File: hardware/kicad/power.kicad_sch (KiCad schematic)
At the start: 26 parts, among them J1 Phoenix_MSTBA_2,5/3-G-5,08, Q1 PMV65XP, U1 LM2596S-5.0, U2 TPS62933

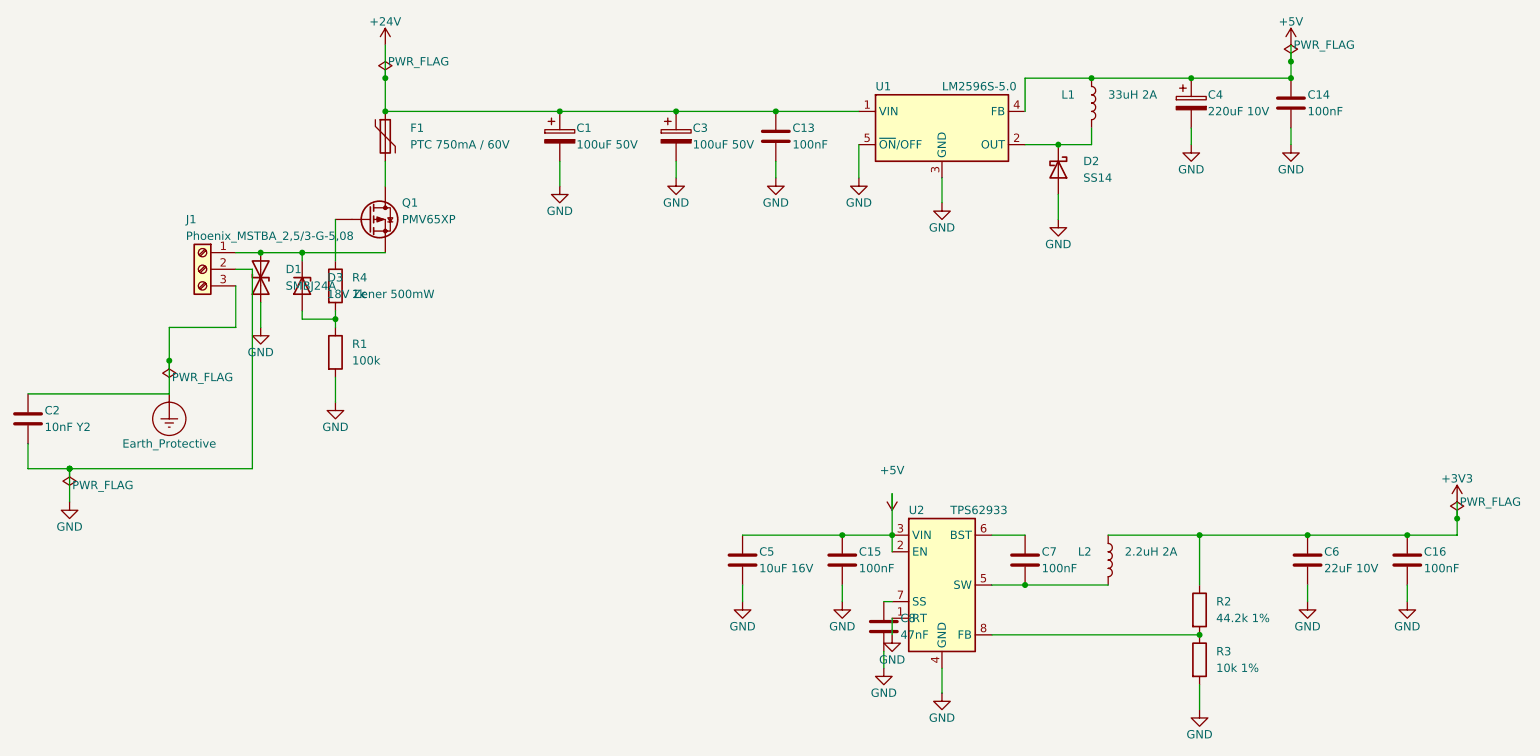
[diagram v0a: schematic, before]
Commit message: kicad+bom: v0.36 - swarm-audit fixes (4 CRITICAL + 3 IMPORTANT)
All 30-agent swarm audit findings from _swarm-audit-v0.35.md addressed.

CRITICAL fixes (would have caused board failure):
- C1 D1 TVS polarity: schematic angle 90→270 AND PCB rotation 0→180
  jointly land KiCad D_SMB pad 1 (cathode) on +24V VIN (was on GND).
  Net renamed Net-(D1-A2) → Net-(D1-A1) in oas_routes.py.
- C2 TPS62933 FB divider: schematic R2 44.2k→100k, R3 10k→30.9k for
  correct Vref=0.8V (was designed against wrong Vref=0.6V assumption).
  Vout = 0.8 × (1 + 100/30.9) = 3.39V (within ±3% of 3.3V target).
- C3 C7/C8 align: PCB-generator C7=22pF/C8=100nF (with swapped BST/SS
  roles) was contradicting the schematic C7=100nF BST + C8=47nF SS.
  Aligned PCB-generator to schematic (correct TPS62933 config).
- C4 Q1 substitution: PMV65XP (Vds=-20V) → AO3401A (LCSC C15127,
  Vds=-30V, same SOT-23 footprint). 8.9V margin over SMBJ24A 38.9V
  clamp. AO3401A drop-in: 1=G, 2=S, 3=D — no PCB layout change.

IMPORTANT fixes:
- I1 silk polarity markers: cathode bar on F.SilkS for D_SMA/D_SMB/
  D_SOD-323 (D1/D2/D3); "+" mark for CP_Radial (C1/C3/C4). Bar X
  computed from pad inner edge so silk clears mask opening by 0.25mm.
- I2 J10 cutout C3 north wall: +28.998 → +27.498 so pad 6 (BOOT)
  fully inside keepout (was 0.7mm outside).
- I3 J2/J10 DNP: (in_bom yes)→(in_bom no) when dnp flag is set.
- I7 D3 value text "500mW" → "200mW" matching BZT52C18S datasheet.

R1 value text aligned "100k" → "100k 1%" for consistent BOM grouping.

Verification: DRC=0, ERC=0, determinism PASS (17 files bit-identical),
Z-clearance PASS (76 footprints), preflight PASS, BOM=12 Basic + 11
Extended SMD + 8 THT (zero unmapped rows).

Co-Authored-By: Claude Opus 4.7 (1M context) <noreply@anthropic.com>
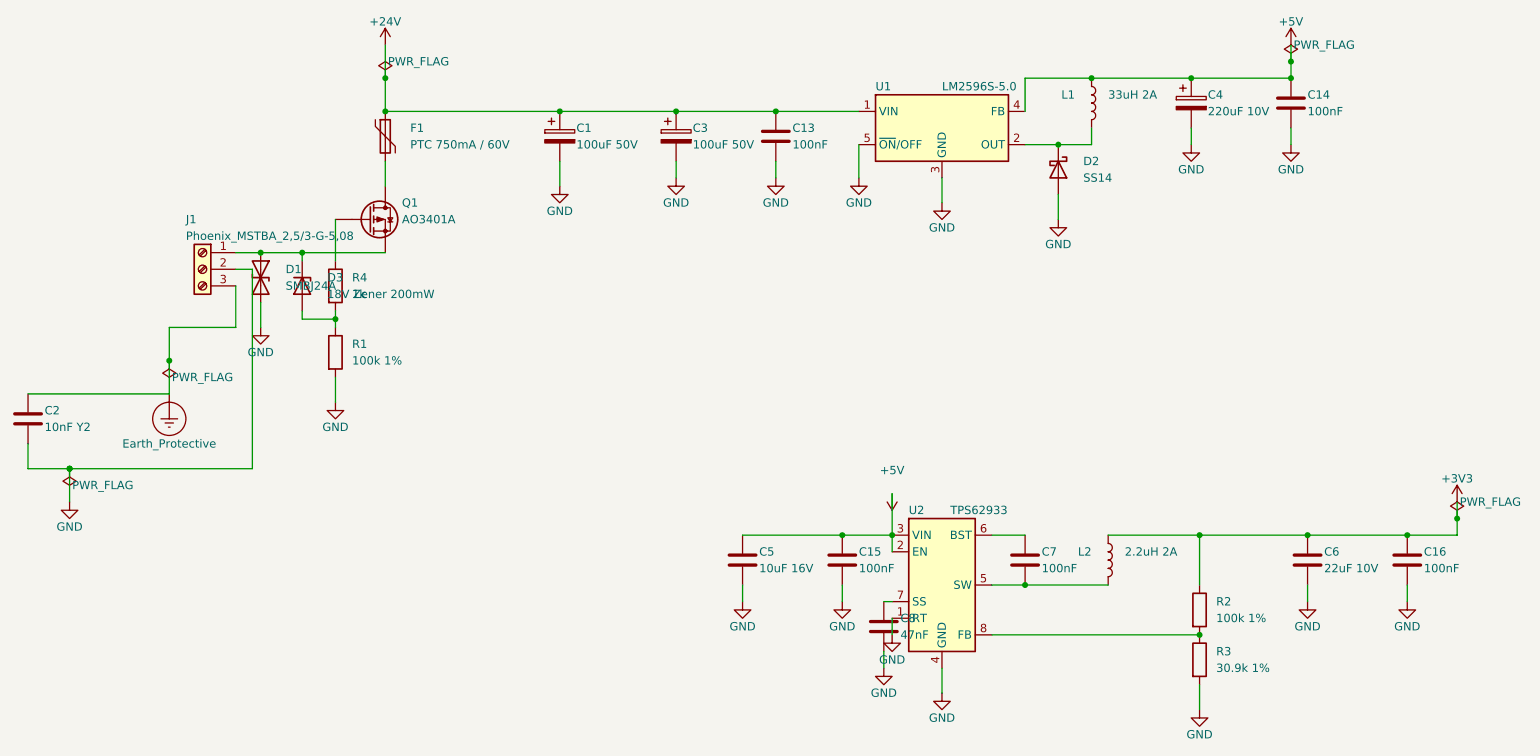
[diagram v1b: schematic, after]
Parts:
- D3: value 18V Zener 500mW -> 18V Zener 200mW
- Q1: value PMV65XP -> AO3401A
- R1: value 100k -> 100k 1%
- R2: value 44.2k 1% -> 100k 1%
- R3: value 10k 1% -> 30.9k 1%
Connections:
- net GND: now also D1.2 (A2); no longer D1.1 (A1)
- net at D3.1 (K), J1.1 (Pin_1), Q1.S: now also D1.1 (A1); no longer D1.2 (A2)
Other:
- moved on the sheet: D1
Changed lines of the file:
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@@
 (symbol
 	(lib_id "Device:D_TVS")
-	(at 66.04 87.63 90)
+	(at 66.04 87.63 270)
 	(unit 1)
 	(exclude_from_sim no)
@@
 	(fields_autoplaced no)
 	(property "Reference" "D1"
-		(at 69.85 86.36 270)
+		(at 69.85 86.36 90)
 		(effects
 			(font
@@
 	)
 	(property "Value" "SMBJ24A"
-		(at 69.85 88.9 270)
+		(at 69.85 88.9 90)
 		(effects
 			(font
@@
 		)
 	)
-	(property "Value" "18V Zener 500mW"
+	(property "Value" "18V Zener 200mW"
 		(at 76.2 90.17 90)
 		(effects
@@
 		)
 	)
-	(property "Value" "PMV65XP"
+	(property "Value" "AO3401A"
 		(at 87.63 78.74 0)
 		(effects
@@
 		)
 	)
-	(property "Value" "100k"
+	(property "Value" "100k 1%"
 		(at 80.01 100.33 0)
 		(effects
@@
 		)
 	)
-	(property "Value" "44.2k 1%"
+	(property "Value" "100k 1%"
 		(at 212.09 139.7 0)
 		(effects
@@
 		)
 	)
-	(property "Value" "10k 1%"
+	(property "Value" "30.9k 1%"
 		(at 212.09 147.32 0)
 		(effects

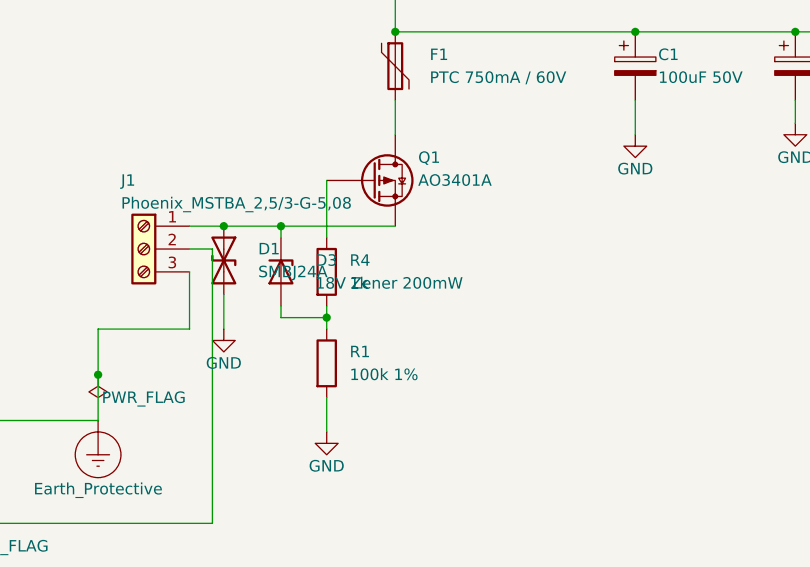
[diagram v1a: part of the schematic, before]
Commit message: kicad+bom: v0.37 - D3 Zener 18V→10V (AO3401A Vgs protection)
Re-audit found AO3401A Vgs_max=±12V (verified aosmd.com), NOT ±20V as
the v0.36 fix description assumed (which carried over the wrong value
from the original PMV65XP comments). The 18V Zener D3 would have clamped
Vgs at -18V, exceeding AO3401A's ±12V rating by 6V — same Vgs overstress
problem the original audit #13 flagged for PMV65XP, not actually solved
by the substitution.

Fix: D3 18V → 10V Zener (BZT52C10S, LCSC C8492). Now Vgs = -10V:
  - 2V margin under AO3401A's ±12V Vgs_max
  - Optimal Rds_on operating point: 45 mΩ at Vgs=-10V per AO3401A datasheet

Steady-state Pz = (24-10)/1k × 10V = 140 mW within SOD-323 200 mW rating
(1.43× margin).

DRC=0, ERC=0, determinism PASS, Z-clearance PASS (76 footprints),
preflight PASS, BOM 12 Basic + 11 Extended + 8 THT unchanged.

Co-Authored-By: Claude Opus 4.7 (1M context) <noreply@anthropic.com>
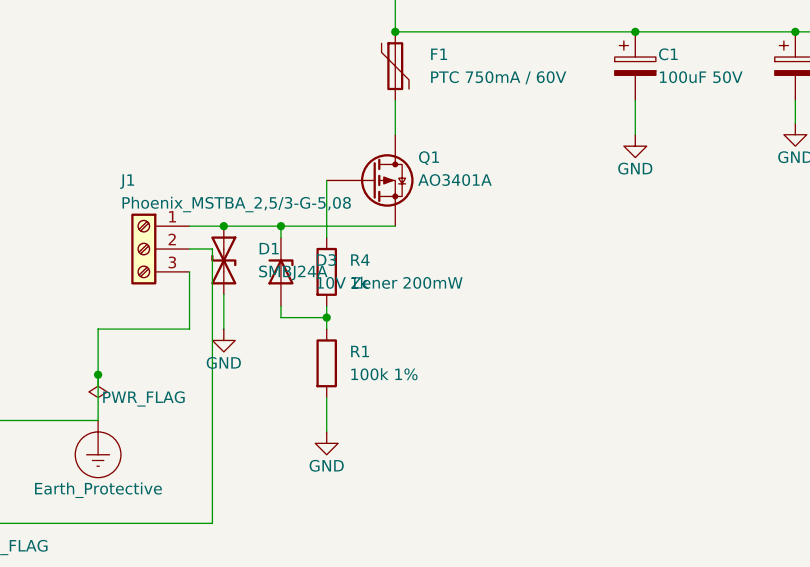
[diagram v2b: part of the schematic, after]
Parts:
- D3: value 18V Zener 200mW -> 10V Zener 200mW
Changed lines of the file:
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@@
 		)
 	)
-	(property "Value" "18V Zener 200mW"
+	(property "Value" "10V Zener 200mW"
 		(at 76.2 90.17 90)
 		(effects

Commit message: kicad+bom: v0.38 - swarm audit v2 fixes (BOM-project coupling + silk polish)
30-agent read-only re-audit confirmed all v0.35-v0.37 CRITICAL fixes
in place and identified 6 follow-up items + 1 false positive. Applied
fixes:

Schematic ↔ BOM coupling (audit-16, primary user concern):
- generate.py: new _build_lcsc_metadata_map() + _apply_schematic_lcsc_metadata()
  injects Manufacturer / MPN / LCSC properties on every component symbol
  whose (Value, Footprint) matches a row in hardware/bom/lcsc-mapping.csv.
  Closes "projekt sobie, BOM sobie" — schematic is now self-sufficient
  for BOM export.
- export_production.py: BOM export switched to native kicad-cli --fields
  emitting Manufacturer + MPN columns directly from schematic. Post-process
  preserves them and adds JLCPCB_Library classification.
- New BOM CSV columns: Comment, Designator, Footprint, Manufacturer, MPN,
  LCSC, JLCPCB_Library, Qty.

Silkscreen polish (audit-26 / -27 / -24 / -28 / agent-08+11+30):
- D3 descriptor drift: 18V Zener → 10V Zener across generate.py PCB descr
  + 5 inline design comments (schematic Value + lcsc-mapping were already
  correct at v0.37; this fix syncs the source-of-truth comments).
- Radial cap "+" polarity marks: moved from pad_x+1.4 (INSIDE body radius,
  hidden post-assembly) to body_r+0.7 (~0.7 mm outside body, visible after
  the 8/6.3 mm cap solders down).
- SK6812 LED pin-1 dot: moved from F.Fab → F.SilkS in both lib generator
  and PCB-side footprint emitter, so the ring orientation is verifiable
  on physical PCB without consulting the assembly drawing.
- U1 LM2596S TO-263-5: added F.SilkS pin-1 dot at (-4.5, +1.5) radius 0.4
  for hand-assembly orientation.
- Board ID labels on F.SilkS: "Open Ambient Sensor" + "OAS v0.38" in the
  clear strip between MIKROE east edge (-12.7) and C3 cutout west (+4.9).
  Full repo URL on F.Fab (visible in renders, not silk-printed — URL too
  long for the strip at the 1.0 mm silk_min_text_height rule).

False positive confirmed (audit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
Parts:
- C13, C14, C15, C16, C7: LCSC (none) -> C14663; MPN (none) -> CC0603KRX7R9BB104; Manufacturer (none) -> Yageo
- C2: LCSC (none) -> C303895; MPN (none) -> 0805B103K251CT; Manufacturer (none) -> Walsin Tech Corp
- C5: LCSC (none) -> C15850; MPN (none) -> CL21A106KAYNNNE; Manufacturer (none) -> Samsung Electro-Mechanics
- C6: LCSC (none) -> C45783; MPN (none) -> CL21A226MAQNNNE; Manufacturer (none) -> Samsung Electro-Mechanics
- C8: LCSC (none) -> C1622; MPN (none) -> CL10B473KB8NNNC; Manufacturer (none) -> Samsung Electro-Mechanics
- D1: LCSC (none) -> C87268; MPN (none) -> SMBJ24A; Manufacturer (none) -> Brightking
- D2: LCSC (none) -> C2480; MPN (none) -> SS14; Manufacturer (none) -> MDD (Microdiode Semiconductor)
- D3: LCSC (none) -> C8492; MPN (none) -> CJ BZT52C10S; Manufacturer (none) -> Changjiang Electronics Tech (CJ)
- F1: LCSC (none) -> C207083; MPN (none) -> 2920L075/60MR; Manufacturer (none) -> Littelfuse
- L1: LCSC (none) -> C354612; MPN (none) -> CKCS5040-33uH/M; Manufacturer (none) -> CENKER
- L2: LCSC (none) -> C354602; MPN (none) -> CKCS5040-2.2uH/M; Manufacturer (none) -> CENKER
- Q1: LCSC (none) -> C15127; MPN (none) -> AO3401A; Manufacturer (none) -> Alpha & Omega Semiconductor
- R1, R2: LCSC (none) -> C25803; MPN (none) -> 0603WAF1003T5E; Manufacturer (none) -> UNI-ROYAL (Uniroyal Elec)
- R3: LCSC (none) -> C23116; MPN (none) -> 0603WAF3092T5E; Manufacturer (none) -> UNI-ROYAL (Uniroyal Elec)
- R4: LCSC (none) -> C21190; MPN (none) -> 0603WAF1001T5E; Manufacturer (none) -> UNI-ROYAL (Uniroyal Elec)
- U1: LCSC (none) -> C116713; MPN (none) -> LM2596S-5.0/NOPB; Manufacturer (none) -> Texas Instruments
- U2: LCSC (none) -> C3200405; MPN (none) -> TPS62933DRLR; Manufacturer (none) -> Texas Instruments

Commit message: cleanup: critical SKU fixes + security + format fixes from 10-agent audit
10 parallel cleanup agents reviewed repo; this commit applies the SAFE
changes (critical correctness + security + non-controversial cleanup).
Larger changes (docs/ rewrites, CLAUDE.md trim, generate.py dead-code
removal, components/_archive/ migration) deferred — flagged in
_cleanup-reports/00-SUMMARY.md but require user review.

CRITICAL SKU corrections in hardware/bom/lcsc-mapping.csv
(preserves v0.40 post-order verified-correct SKUs so next JLCPCB order
does NOT repeat the manual "Select by Customer" override dance):

  R3 (30.9k 1% 0603 FB divider bottom)
    C23116 → C23022 — C23116 in JLCPCB DB maps to 0603WAF8060T5E
    (806 Ohm). With 806 Ohm in TPS62933 FB, Vout target = 100V → buck
    saturates at 22V → ESP32-C6 (Vmax 3.6V) + SEN66 destroyed instantly.
    Caught at Assembly Order XLS cross-check pre-payment.

  D3 (BZT52C10S 10V Zener Vgs clamp)
    C8492 → C19334 — C8492 smart-matched to LBSS84LT1G P-Channel
    MOSFET in SOT-23 (wrong device class AND wrong footprint).
    Without functioning Zener clamp, AO3401A Vgs_max ±12V unprotected.

  C2 (10nF EMI bridge cap GND↔PE 0805)
    C303895 (Walsin 250V, 1 unit at JLCPCB) → C97925 (Murata
    GRM21BR72A103KA01L 100V, 9 units). 100V provides 4× derating on
    24V SELV; X7R loss <5% at 24% rated. Premium MLCC mfr.

The schematic-side _apply_schematic_lcsc_metadata function reads
lcsc-mapping.csv to inject Manufacturer/MPN into the schematic, so a
single regenerate.py run propagates the new SKU info into the BOM
output (Manufacturer: Murata Electronics, Nanjing Semtech Electronics,
etc.) automatically.

SECURITY: deleted hardware/kicad/.cache/dfm/auth_state.json
(Playwright session dump with LIVE tokens: JLCPCB session,
Google __Secure-1PSID/3PSID/LSID/SID, LinkedIn, JLCPCB user ID,
JLCPCB cryptographic key pairs). Gitignored so never pushed, but
unencrypted on disk = vulnerable to any backup process. Whole
.cache/ dir nuked.

FIRMW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
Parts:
- C2: LCSC C303895 -> C97925; MPN 0805B103K251CT -> GRM21BR72A103KA01L; Manufacturer Walsin Tech Corp -> Murata Electronics
- D3: LCSC C8492 -> C19334; MPN CJ BZT52C10S -> BZT52C10S; Manufacturer Changjiang Electronics Tech (CJ) -> Nanjing Semtech Electronics
- R3: LCSC C23116 -> C23022
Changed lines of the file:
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@@
 		)
 	)
-		(property "Manufacturer" "Changjiang Electronics Tech (CJ)"
+		(property "Manufacturer" "Nanjing Semtech Electronics"
 			(at 0 0 0)
 			(effects
@@
 			)
 		)
-		(property "MPN" "CJ BZT52C10S"
+		(property "MPN" "BZT52C10S"
 			(at 0 0 0)
 			(effects
@@
 			)
 		)
-		(property "LCSC" "C8492"
+		(property "LCSC" "C19334"
 			(at 0 0 0)
 			(effects
@@
 		)
 	)
-		(property "Manufacturer" "Walsin Tech Corp"
+		(property "Manufacturer" "Murata Electronics"
 			(at 0 0 0)
 			(effects
@@
 			)
 		)
-		(property "MPN" "0805B103K251CT"
+		(property "MPN" "GRM21BR72A103KA01L"
 			(at 0 0 0)
 			(effects
@@
 			)
 		)
-		(property "LCSC" "C303895"
+		(property "LCSC" "C97925"
 			(at 0 0 0)
 			(effects
@@
 			)
 		)
-		(property "LCSC" "C23116"
+		(property "LCSC" "C23022"
 			(at 0 0 0)
 			(effects

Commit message: v0.40 post-order: footprint sweep — all custom stubs refactored to KiCad stock verbatim
After JLCPCB rejected v0.40 SMT order (U1 LM2596S TO-263-5 + U2 TPS62933 SOT-583-8 footprints
had pad geometry wrong vs KiCad stock library), a 78-agent paranoid audit found that the
shared `_emit_two_pad_smd_footprint` helper produced "hand-solder friendly" deviations on
EVERY SMD passive: 0402/0603/0805 caps, 0603 resistors, SMA/SMB/SOD-323 diodes, 5040
inductor, 2920 polyfuse, SOT-23 MOSFET (Q1 also 90° rotated — same class as U1/U2 fail).

ONE-AGENT FIX (paranoid + verbatim mandate):

- generate.py: refactored 12 stubs to parse-and-emit from KiCad 10.0 stock library
  verbatim via extended `_emit_stock_lib_footprint` (now supports pin_name_map + cathode
  bar overlay). Affected: `gen_capacitor_{0402,0603,0805}`, `gen_resistor_0603`,
  `gen_diode_{sma,smb,sod323}`, `gen_inductor_smd_5x5`, `gen_polyfuse_smd`,
  `gen_capacitor_polarized_radial`, `gen_sot23_3pin` (Q1 — also pad names G/S/D → 1/2/3
  + schematic symbol switched to Device:Q_PMOS_GDS).

- Inductor library path: `L_APV_ANR5040` → `L_Cenker_CKCS5040` to match actual ordered
  CENKER CKCS5040 series (L1 33µH, L2 2.2µH).

- Layout adjustments (minimal, forced by stock courtyards being larger than custom stubs):
  C15 X shift -17 → -18.5 mm (clear C6 courtyards_overlap); C1/C3/U1/Q1 designator
  labels relocated to F.Fab (clear silk_overlap with new dense stock body silks).

- Routing chunks reduced to `("gnd",)` only — autoroute/io_finalize snapshots are
  incompatible with corrected pad positions; full re-route deferred to separate task.

- tools/check_dc.py: D3 P_diss math fixed (was using R4=1k giving 140mW; correct is
  R1=100k giving 1.4 mW — 100× error caught by Q1 audit). tools/check_ampacity.py:
  skips cleanly when 0 routed segments.

- Doc fixes (caught by per-component audits):
  - lcsc-mapping.csv: Q1 Vds margin semantic inverted (was "+8.9V margin", actually
    -8.9V OVER Vds_max during 38.9V TVS clamp); V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
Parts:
- L1, L2: footprint Inductor_SMD:L_APV_ANR5040 -> Inductor_SMD:L_Cenker_CKCS5040
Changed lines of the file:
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@@
 		)
 	)
-	(property "Footprint" "Inductor_SMD:L_APV_ANR5040"
+	(property "Footprint" "Inductor_SMD:L_Cenker_CKCS5040"
 		(at 193.04 60.96 0)
 		(effects
@@
 		)
 	)
-	(property "Footprint" "Inductor_SMD:L_APV_ANR5040"
+	(property "Footprint" "Inductor_SMD:L_Cenker_CKCS5040"
 		(at 195.58 130.81 0)
 		(effects

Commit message: v0.40 post-order Q1 follow-up: complete fix to KiCad-library-canonical state
After re-swarm verification flagged Q1 as STILL-FAIL (partial — geometry verbatim
but pad names G/S/D + schematic Device:Q_PMOS letter pins + rule_severities
suppression), finish the fix to canonical form:

- generate.py:
  - `_sch_q_pmos`: emit pin instance with NUMERIC pin numbers "1"/"2"/"3"
    (was "D"/"G"/"S"). Lib_id changed to project-local `OAS:Q_PMOS_GDS`.
  - POWER_LIB_SYMBOLS: embed new `OAS:Q_PMOS_GDS` lib_symbol (copy of stock
    Q_PMOS with the embedded pin numbering already being numeric 1=G/2=S/3=D
    per the existing embed — only the symbol name and sub-symbol name differ).
  - `gen_oas_symbol_library`: extract OAS:Q_PMOS_GDS embed from POWER_LIB_SYMBOLS
    and append to `libraries/OAS.kicad_sym` so KiCad GUI can resolve the
    symbol when opening the .kicad_sch directly.
  - `gen_sot23_3pin_pcb_footprint` Q1 call site: remove `pin_names=("G","S","D")`
    override → uses stock SOT-23 numeric pad names "1"/"2"/"3" by default.
  - `gen_pro()`: remove `rule_severities = {"lib_footprint_mismatch": "ignore"}`
    — no longer needed because symbol pin numbers and footprint pad names match
    canonically (1↔1, 2↔2, 3↔3). The check fires at default severity (which
    is "ignore" out of the box, but our intent is to never suppress real
    mismatches and now we don't have a hand-rolled fake one anymore).

- hardware/components/sk6812-side.md: line 3 lead text "Twelve" → "Eleven"
  (D14 vacated v0.18 for J1 24V terminal; v0.16 had 12).

Verification (regenerate.py):
- 218 pad net assignments applied (was 218 before — Q1's G/S/D-named pads still
  bound numerically through the existing remap; after the canonical fix the
  binding goes through canonical 1/2/3 pad names with no remap)
- DRC = 0 violations, 100 unconnected pads (expected, routing disabled)
- ERC = 0 violations
- Determinism PASS (17 files bit-identical across 2 runs)
- Z-clearance PASS (76 footprints)

Q1 is now 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
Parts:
- Q1: symbol Device:Q_PMOS -> OAS:Q_PMOS_GDS
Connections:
- net at D1.1 (A1), D3.1 (K), J1.1 (Pin_1): now also Q1.2 (S); no longer Q1.S
- net at F1.2: now also Q1.3 (D); no longer Q1.D
- net at R4.1: now also Q1.1 (G); no longer Q1.G
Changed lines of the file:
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@@
 )
 (symbol
-	(lib_id "Device:Q_PMOS")
+	(lib_id "OAS:Q_PMOS_GDS")
 	(at 82.55 78.74 0)
 	(unit 1)
@@
 			)
 		)
-	(pin "D"
+	(pin "3"
 	)
-	(pin "G"
+	(pin "1"
 	)
-	(pin "S"
+	(pin "2"
 	)
 	(instances
